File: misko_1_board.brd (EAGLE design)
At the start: 115 x 115 mm, 152 parts, among them IC1 ATMEGA1281-16AU, IC10 ORG1510-MK4, IC11 TPS3808G33DBVT, IC12 LTC4425, IC13 RN4678_BT_MODULE, IC14 ADXL345, IC15 74HCT1G32, IC16 FM25W256-SOIC, IC17 MICROSD_SPI_MODE, IC18 FH12-30S-0.5SH, IC19 DS1394U-33+, IC2 MC1525TT, IC20 ATWINC1500-MR210PB, IC21 115Q-BCA0, IC22 SIM800, IC23 SP3012-04UTG, IC3 TMP36GRTZ, IC4 TPS63031, IC5 MCP73871-2AAI/ML, IC6 MAX6818, IC7 FT230XS, IC8 SN74LVC1G3157DBVR - BT switch, IC9 SN74LVC1G3157DBVR - GPS switch, Q1 ABM3B-8MHZ-10-1-U-T, Q2 LFXTAL016178R, SW1 RESET, SW2 POWER SWITCH, SW3 MICROJOYSTICK, SW4 PB6156RSL, SW5 PB6156RSL, T1 BSS84

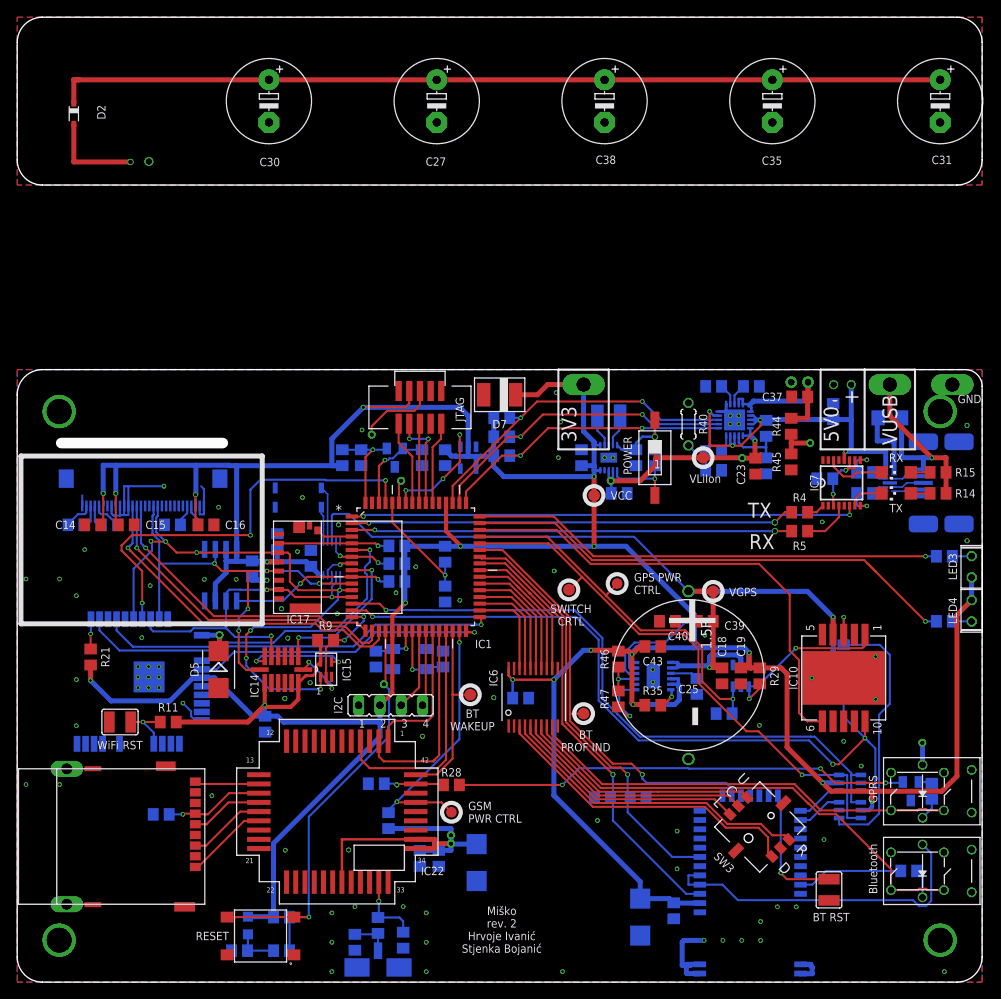
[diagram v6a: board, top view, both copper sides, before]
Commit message: - removed GSM and WiFi modules & adapted schematic and board accordingly - rerouted int lines for accelerometer and RTC to INT0 and 1, respectively (freed up PE7 and PE6, respectively
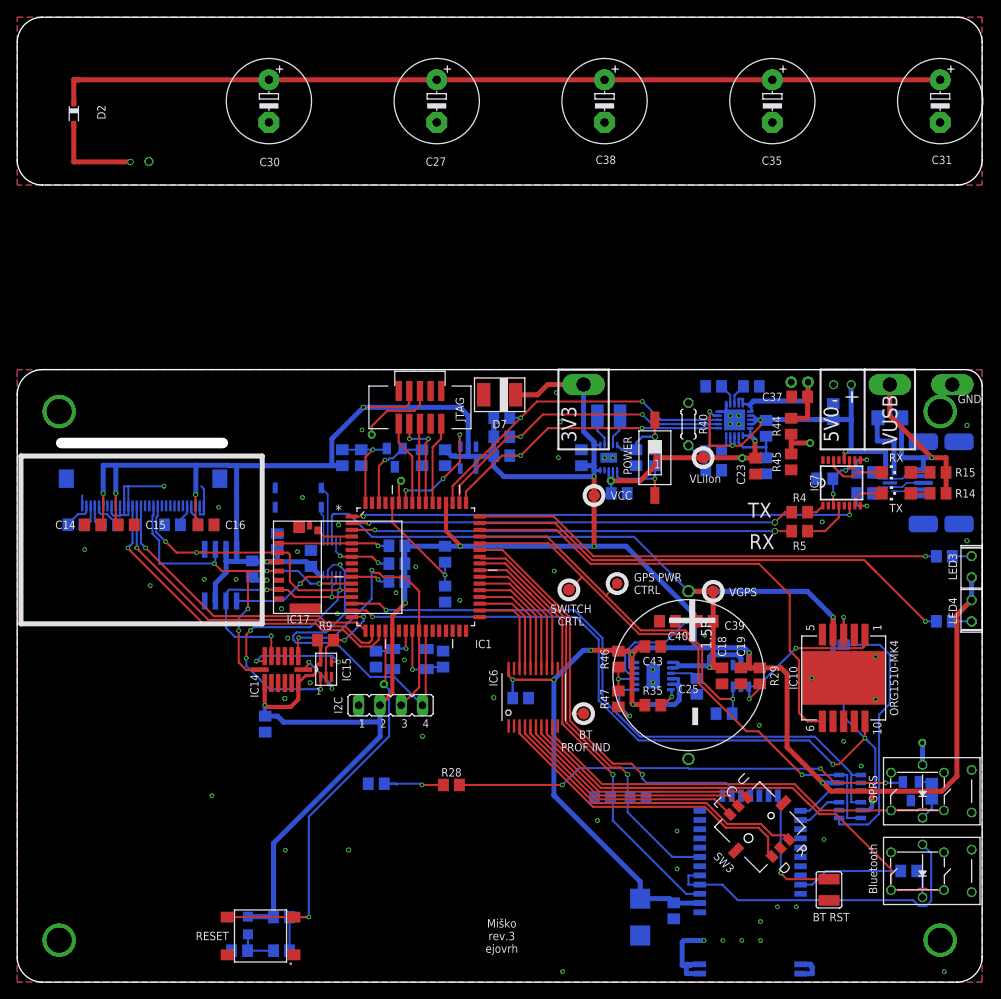
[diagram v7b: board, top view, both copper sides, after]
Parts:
- removed C22, C28, C33: 10µF, rcl:C0805
- removed C24: 10pF, rcl:C0805
- removed C26: 33pF, rcl:C0805
- removed CONN5: U.FL-R-SMT 1, discrete:SMD
- removed D3, D5: SZ1SMB5916BT3G, diode:SMB
- removed IC20: ATWINC1500-MR210PB, ATWINC1500-MR210PB WiFi Module:SMT
- removed IC21: 115Q-BCA0, 115Q-BCA0 Micro-SIM Socket:115Q-BCA0
- removed IC22: SIM800, SIM800 GPRS Module:SIM800C
- removed R11: 10k, rcl:R0805
- removed R21: 1M, rcl:R0805
- removed R31: 47k, resistor:R0805
- removed R38: 1k, rcl:R0805
- removed SJ1: WiFi RST, jumper:SJW
- removed TP10: Bluetooth Wakeup Pin, testpad:TP14R
- removed TP9: SIM800 Power CTRL Pin, testpad:B1,27
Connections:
- removed net ANTENNA: C33.2, CONN5.SIGNAL, R38.2
- removed net GSM_ANT: C28.2, IC22.GSM_ANT, R38.1
- removed net I2C_SCL_PIN: CONN2.3, IC1.25
- removed net I2C_SDA_PIN: CONN2.4, IC1.26
- removed net N$15: IC20.RESET_N, R11.1, SJ1.1
- removed net SIM800C_CTS_PIN: IC1.29, IC22.UART1_CTS
- removed net SIM800C_POWER_CTRL_PIN: IC1.30, IC22.STATUS, TP10.TP
- removed net SIM800C_POWER_PIN: IC1.31, IC22.PWRKEY, R31.1, TP9.TP
- removed net SIM800C_RX_PIN: IC1.27, IC22.UART1_TXD
- removed net SIM800C_TX_PIN: IC1.28, IC22.UART1_RXD
- removed net SIM_CLOCK: IC21.CLK, IC22.SIM_CLK
- removed net SIM_DATA: C22.1, IC21.I/O, IC22.SIM_DATA
- removed net SIM_DETECT: IC21.CD, IC22.SIM_DET
- removed net SIM_RESET: IC21.RST, IC22.SIM_RST
- removed net SIM_VDD: IC21.VCC, IC22.SIM_VDD
- removed net SPI_CFG: IC20.SPI_CFG, R21.2
- removed net SPI_SS_WIFI_MODULE: IC1.61, IC20.SPI_SSN
- removed net WIFI_EN_PIN: IC1.32, IC20.CHIP_EN
- removed net WIFI_IRQ_PIN: IC1.6, IC20.IQRN
- removed net WIFI_WAKE_PIN: IC1.33, IC20.WAKE
- new net UART1_GPS_RX: IC1.27
- new net UART1_GPS_TX: IC1.28
- net ADXL345_INT1_INTERRUPT_PIN: now also CONN2.3, IC1.25; no longer IC1.9
- net GND: no longer C22.2, C24.1, C26.1, C28.1, C33.1, CONN5.GND1, CONN5.GND2, D3.A, D5.A, IC20.GND1, IC20.GND10, IC20.GND11, IC20.GND12, IC20.GND13, IC20.GND2, IC20.GND3, IC20.GND5, IC20.GND6, IC20.GND7, IC20.GND8, IC20.GND9, IC20.PADDLE, IC21.GND1, IC21.GND2, IC21.GND3, IC21.GND4, IC21.GND5, IC21.GND6, IC21.GND7, IC22.GND10, IC22.GND2, IC22.GND3, IC22.GND4, IC22.GND6, IC22.GND7, IC22.GND8, IC22.GND9, SJ1.2
- net GPRS_NETLIGHT: no longer IC22.NETLIGHT
- net RTC_INT_INTERRUPT_PIN: now also CONN2.4, IC1.26; no longer IC1.8
- net SPI_MISO_PIN: no longer IC20.SPI_MISO
- net SPI_MOSI_PIN: no longer IC20.SPI_MOSI
- net SPI_SCK_PIN: no longer IC20.SPI_SCK
- net VCC: no longer IC20.VDDIO, R11.2, R21.1
- net V_LIION+: no longer C24.2, C26.2, D3.C, D5.C, IC20.VBAT, IC22.VBAT1, IC22.VBAT2, IC22.VRTC, R31.2
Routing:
- net SPI_SS_WIFI_MODULE: track 50.4 -> 0.00 mm, vias 3 -> 0
- net WIFI_WAKE_PIN: track 50.1 -> 0.00 mm, vias 1 -> 0
- net WIFI_IRQ_PIN: track 44.6 -> 0.00 mm, vias 1 -> 0
- net V_LIION+: track 61.7 -> 19.3 mm, vias 3 -> 0
- net RTC_INT_INTERRUPT_PIN: track 3.81 -> 44.0 mm
- net VCC: track 517.9 -> 479.8 mm, vias 19 -> 18
- net WIFI_EN_PIN: track 35.4 -> 0.00 mm, vias 1 -> 0
- net SIM800C_POWER_PIN: track 32.3 -> 0.00 mm, vias 2 -> 0
- net SIM800C_CTS_PIN: track 28.6 -> 0.00 mm
- net SIM800C_TX_PIN: track 24.6 -> 0.00 mm
- net SIM800C_POWER_CTRL_PIN: track 22.6 -> 0.00 mm
- net ADXL345_INT1_INTERRUPT_PIN: track 18.7 -> 37.5 mm
- net SIM800C_RX_PIN: track 17.8 -> 0.00 mm
- net SPI_MOSI_PIN: track 75.4 -> 63.4 mm, vias 7 -> 6
- net SIM_DATA: track 11.8 -> 0.00 mm, vias 1 -> 0
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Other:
- board text added: "Miško rev.3 ejovrh"
- board text removed: "BT WAKEUP"
- board text removed: "GSM PWR CTRL"
- board text removed: "Miško rev. 2 Hrvoje Ivanić Stjenka Bojanić"
- board text removed: "WiFi RST"
